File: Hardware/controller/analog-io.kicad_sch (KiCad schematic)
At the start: 9 parts

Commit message: Replaced most passives with 0603 size
- This is more compact, and we might as well since this board will be at
  least partially assembled beforehand
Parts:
- U: MPN CL21B104KACNFNC -> (none)
- U: MPN RMC1/10-222JTP -> (none)
- U: MPN RMC1/10-103JTP -> (none)
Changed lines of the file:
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@@
       (effects (font (size 1.27 1.27)) hide)
     )
-    (property "MPN" "CL21B104KACNFNC" (id 4) (at 69.85 40.005 0)
+    (property "MPN" "" (id 4) (at 69.85 40.005 0)
       (effects (font (size 1.27 1.27)) hide)
     )
@@
       (effects (font (size 1.27 1.27)) hide)
     )
-    (property "MPN" "RMC1/10-222JTP" (id 4) (at 116.205 50.165 90)
+    (property "MPN" "" (id 4) (at 116.205 50.165 90)
       (effects (font (size 1.27 1.27)) hide)
     )
@@
       (effects (font (size 1.27 1.27)) hide)
     )
-    (property "MPN" "RMC1/10-103JTP" (id 4) (at 116.205 58.42 90)
+    (property "MPN" "" (id 4) (at 116.205 58.42 90)
       (effects (font (size 1.27 1.27)) hide)
     )
@@
       (effects (font (size 1.27 1.27)) hide)
     )
-    (property "MPN" "RMC1/10-222JTP" (id 4) (at 116.205 41.91 90)
+    (property "MPN" "" (id 4) (at 116.205 41.91 90)
       (effects (font (size 1.27 1.27)) hide)
     )

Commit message: Auxiliary I2C + SPI bus routing
- Added an I2C MAC EEPROM to the aux I2C bus, which will be read for the
  device serial and Ethernet MAC address

- Add fan controller, filtering/ESD and fusing for expansion connector
  for rear IO section. We'll still have to add the CAN termination as
  well as the CAN transceiver on that part

- Minor routing + pin location tweaks
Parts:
- U: MPN APA0606220M035R -> A768EB336M1GLAE045
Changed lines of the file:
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@@
       (effects (font (size 1.27 1.27)) hide)
     )
-    (property "MPN" "APA0606220M035R" (id 4) (at 91.44 40.005 0)
+    (property "MPN" "A768EB336M1GLAE045" (id 4) (at 91.44 40.005 0)
       (effects (font (size 1.27 1.27)) hide)
     )

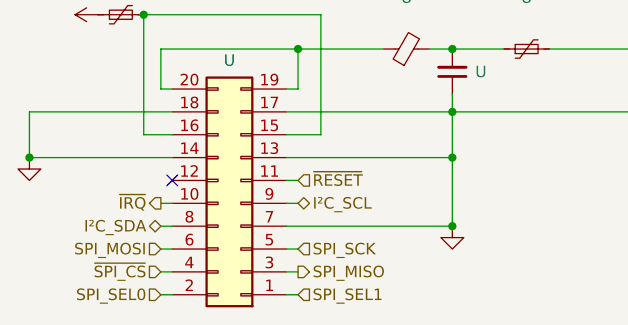
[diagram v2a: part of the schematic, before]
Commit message: Mostly finished up analog load board
- Finished routing most signals

- Connected relay drive to bonus I2C GPIO controller, and routed the
  rest of the voltage sense stuff

- Routed the reset signal to the DAC, so that when the board is reset,
  the current output will be reset to zero as well without processor
  intervention

- Replaced most passives with 0603/1608 size
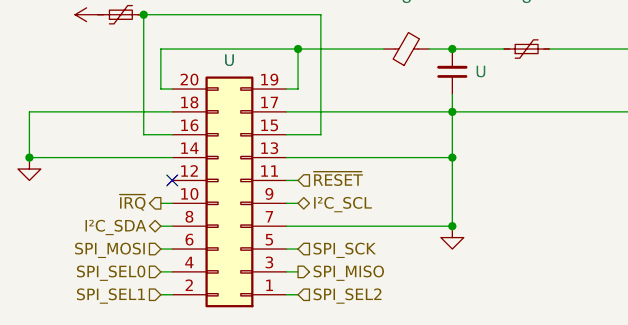
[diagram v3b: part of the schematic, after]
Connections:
- net ~{SPI_CS} is gone; now on net SPI_SEL0: U.4 (Pin_4)
- net SPI_SEL0: no longer U.2 (Pin_2)
- net SPI_SEL1: now also U.2 (Pin_2); no longer U.1 (Pin_1)
- new net SPI_SEL2: U.1 (Pin_1)
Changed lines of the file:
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@@
     (effects (font (size 1.27 1.27)) (justify right))
   )
-  (hierarchical_label "~{SPI_CS}" (shape input) (at 37.465 62.23 180) (fields_autoplaced)
+  (hierarchical_label "SPI_SEL0" (shape input) (at 37.465 62.23 180) (fields_autoplaced)
     (effects (font (size 1.27 1.27)) (justify right))
   )
-  (hierarchical_label "SPI_SEL1" (shape input) (at 52.705 64.77 0) (fields_autoplaced)
+  (hierarchical_label "SPI_SEL2" (shape input) (at 52.705 64.77 0) (fields_autoplaced)
     (effects (font (size 1.27 1.27)) (justify left))
   )
@@
     (effects (font (size 1.27 1.27)) (justify right))
   )
-  (hierarchical_label "SPI_SEL0" (shape input) (at 37.465 64.77 180) (fields_autoplaced)
+  (hierarchical_label "SPI_SEL1" (shape input) (at 37.465 64.77 180) (fields_autoplaced)
     (effects (font (size 1.27 1.27)) (justify right))
   )

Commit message: hw: start working on rev4 controller
- removed SPI for display, and the associated SPI mux nonsense, and any
  superfluous resistors for pull-ups

- removed MAC address EEPROM

- start adding i2c RTC (which will also contain EEPROM with the MAC of
  the system, lol)

- start moving some components from bottom to top side of board

- tweaked positions of some mains voltage traces

- increased values of power indicator LED's current dropping resistors

- take 3V3 from SoM rather than generate it ourselves
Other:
- title: (none) -> Programmable Load Controller
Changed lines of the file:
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@@
 (kicad_sch (version 20220404) (generator eeschema)
   (paper "A4")
+  (title_block
+    (title "Programmable Load Controller")
+    (date "2022-06-28")
+    (rev "4")
+  )
   (junction (at 110.49 50.165) (diameter 0) (color 0 0 0 0)
   )

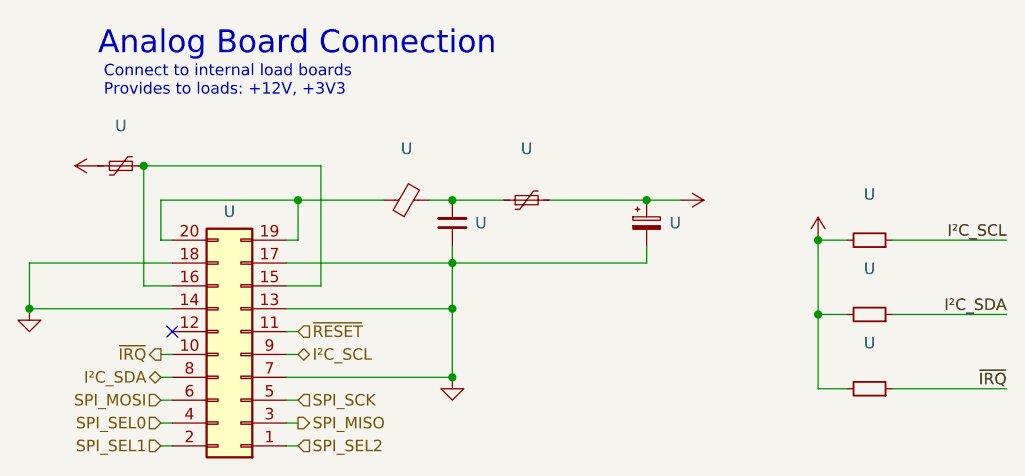
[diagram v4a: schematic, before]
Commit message: hw: revise USB power stuff
- fixed the remaining usb powering stuff for the front panel host
  connector

- replaced 33µF SMD caps with through-hole equivalents

- removed some of the bottom mounted components for analog board power
  connection
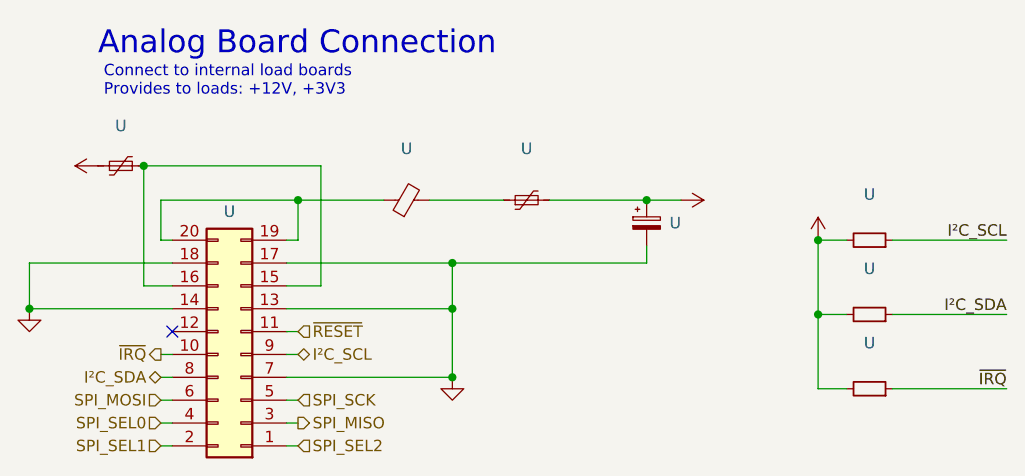
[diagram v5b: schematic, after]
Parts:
- removed U: (no value), symbol Device:C_Small
- U: MPN A768EB336M1GLAE045 -> A758EK226M1EAAE050
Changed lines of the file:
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@@
   (junction (at 52.705 37.465) (diameter 0) (color 0 0 0 0)
-  )
-  (junction (at 69.85 37.465) (diameter 0) (color 0 0 0 0)
   )
   (junction (at 91.44 37.465) (diameter 0) (color 0 0 0 0)
@@
     (stroke (width 0) (type default))
   )
-  (wire (pts (xy 67.31 37.465) (xy 69.85 37.465))
+  (wire (pts (xy 67.31 37.465) (xy 75.565 37.465))
     (stroke (width 0) (type default))
   )
@@
     (stroke (width 0) (type default))
   )
-  (wire (pts (xy 69.85 37.465) (xy 75.565 37.465))
-    (stroke (width 0) (type default))
-  )
   (wire (pts (xy 51.435 46.99) (xy 55.245 46.99))
     (stroke (width 0) (type default))
@@
   )
   (wire (pts (xy 118.745 58.42) (xy 131.445 58.42))
-    (stroke (width 0) (type default))
-  )
-  (wire (pts (xy 69.85 42.545) (xy 69.85 44.45))
     (stroke (width 0) (type default))
   )
@@
     )
     (property "MPN" "MFBM1V2012-800-R" (id 4) (at 64.77 37.465 90)
-      (effects (font (size 1.27 1.27)) hide)
-    )
-    (pin "1")
-    (pin "2")
-  )
-  (symbol (lib_id "Device:C_Small") (at 69.85 40.005 180) (unit 1)
-    (in_bom yes) (on_board yes)
-    (default_instance (reference "U") (unit 1) (value "") (footprint ""))
-    (property "Reference" "U" (id 0) (at 72.39 40.005 0)
-      (effects (font (size 1.27 1.27)) (justify right))
-    )
-    (property "Value" "" (id 1) (at 72.39 42.545 0)
-      (effects (font (size 1.27 1.27)) (justify right))
-    )
-    (property "Footprint" "" (id 2) (at 69.85 40.005 0)
-      (effects (font (size 1.27 1.27)) hide)
-    )
-    (property "Datasheet" "~" (id 3) (at 69.85 40.005 0)
-      (effects (font (size 1.27 1.27)) hide)
-    )
-    (property "MPN" "" (id 4) (at 69.85 40.005 0)
       (effects (font (size 1.27 1.27)) hide)
     )
@@
       (effects (font (size 1.27 1.27)) hide)
     )
-    (property "MPN" "A768EB336M1GLAE045" (id 4) (at 91.44 40.005 0)
-      (effects (font (size 1.27 1.27)) hide)
-    )
+    (property "MPN" "A758EK226M1EAAE050" (id 4) (at 91.44 40.005 0)
+      (effects (font (size 1.27 1.27)) hide)
+    )

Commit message: hw: add charger for RTC
- added RTC supercapacitor

- added the charging circuit for the RTC (with adjustment for voltage
  and all that fun stuff) based around a bonus linear regulator for the
  supercap

- minor tweaks all around: add more JLCPCB part numbers and fixed some
  footprints for some components
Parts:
- U: JLCPCB (none) -> C25804
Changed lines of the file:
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@@
+      (effects (font (size 1.27 1.27)) hide)
+    )
+    (property "JLCPCB" "C25804" (id 5) (at 116.205 58.42 90)
       (effects (font (size 1.27 1.27)) hide)
     )

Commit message: hw: add more jlcpcb p/n; minor cleanup
- added jlcpcb part numbers for various resistors and passives

- minor clean up of stuff on the board, including moving the +VDC
  indicator LED and widening the fastener slot for the RTC supercap
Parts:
- U: JLCPCB (none) -> C4190
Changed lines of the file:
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@@
+      (effects (font (size 1.27 1.27)) hide)
+    )
+    (property "JLCPCB" "C4190" (id 5) (at 116.205 50.165 90)
       (effects (font (size 1.27 1.27)) hide)
     )
@@
       (effects (font (size 1.27 1.27)) hide)
     )
+    (property "JLCPCB" "C4190" (id 5) (at 116.205 41.91 90)
+      (effects (font (size 1.27 1.27)) hide)
+    )

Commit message: hw: fix part numbers
- fixed missing or incorrect MPN and JLCPCB part numbers for various
  components; most should have either one of these now
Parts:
- U: JLCPCB (none) -> C1015
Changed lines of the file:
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@@
+      (effects (font (size 1.27 1.27)) hide)
+    )
+    (property "JLCPCB" "C1015" (id 5) (at 64.77 37.465 90)
       (effects (font (size 1.27 1.27)) hide)
     )
